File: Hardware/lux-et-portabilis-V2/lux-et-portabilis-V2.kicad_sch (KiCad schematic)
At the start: 45 parts, among them J1 Conn_01x03_Socket, J2 Conn_01x03_Socket, J3 Conn_01x04_Socket, Q1 2N7002K, Q2 2N7002K, Q3 PMOS, U1 ESP32-C3-Supermini, U2 TP4056

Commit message: Fabrication files for Lux et Portabilis V2
Added power saving by shutting down the battery
Added onboard boot button
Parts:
- C1, C3: LCSC C2162971 -> C25170691
- C4, C6: LCSC C77075 -> C15850
- C5: LCSC C380331 -> C15850
- D1: LCSC C2909920 -> C2480
- J3: footprint Custom_Footprints:MPU6050 -> Aleoexpress:MPU6050
- PORT1, PORT2: LCSC 1 -> C7433470
- R1, R12, R2: value 2k2 -> 2.2k
- R14, R15: LCSC C60491 -> C149504
- U1: footprint Custom_Footprints:ESP32-C3-Supermini -> Aleoexpress:ESP32-C3-Supermini
- U2: footprint Custom_Footprints:ESOP-8_L4.9-W3.9-P1.27-LS6.0-BL-EP -> Aleoexpress:ESOP-8_L4.9-W3.9-P1.27-LS6.0-BL-EP; Manufacturer Part TP4056 -> (none)

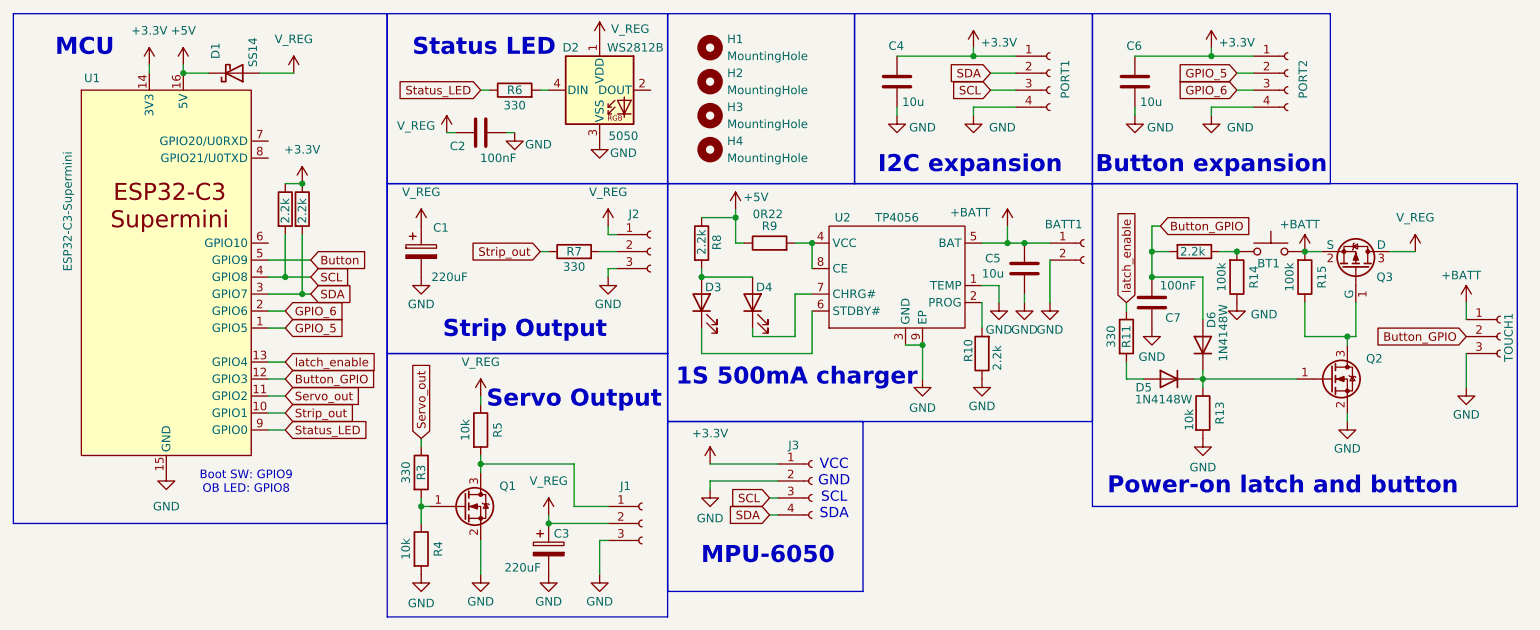
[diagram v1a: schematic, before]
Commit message: Added ADC reading to Portabilis V2
Plus board render
Changed Status LED pin to GPIO10
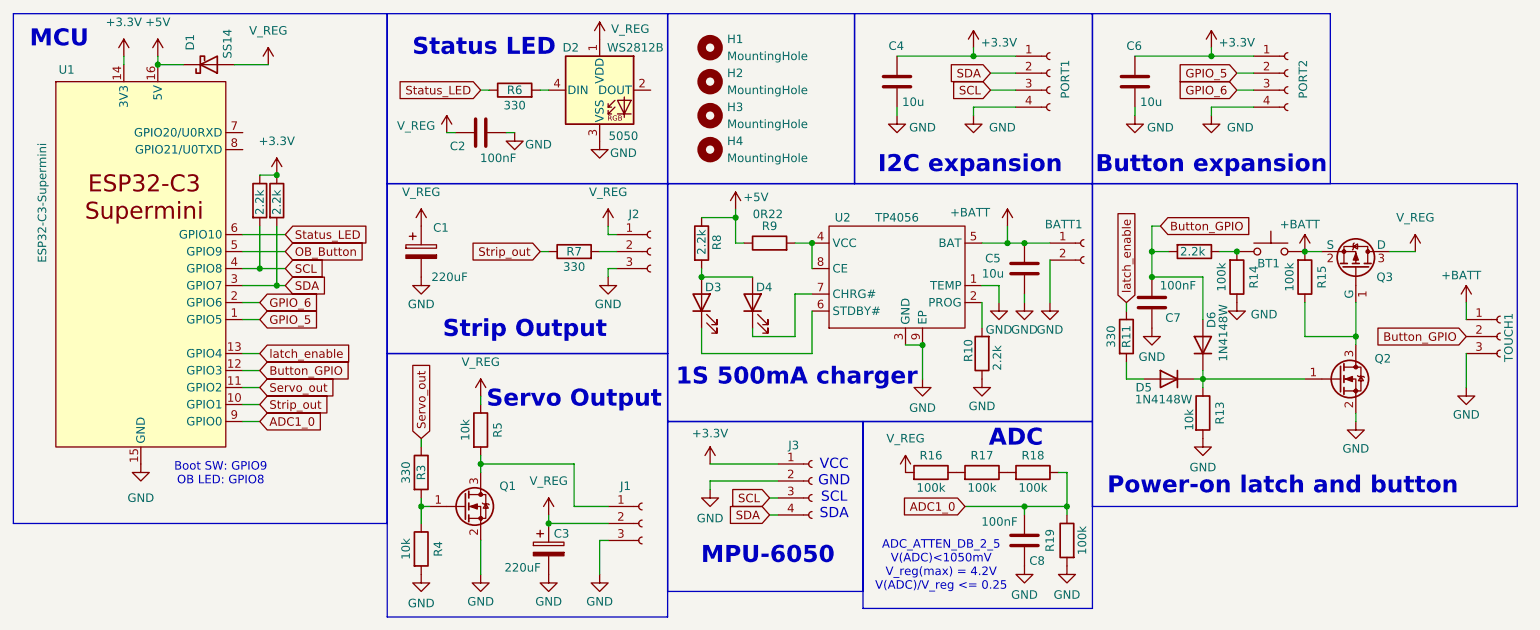
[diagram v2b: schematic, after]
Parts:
- added C8: 100nF, Capacitor_SMD:C_0805_2012Metric, symbol Device:C
- added R16, R17, R18, R19: 100k, Resistor_SMD:R_0805_2012Metric, symbol Device:R
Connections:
- net GND: now also C8.1, R19.2
- net Status_LED: now also U1.6 (GPIO10); no longer U1.9 (GPIO0)
- net V_REG: now also R16.2
- net Button renamed OB_Button
- new net: R17.1, R18.2
- new net: R16.1, R17.2
- new net ADC1_0: C8.2, R18.1, R19.1, U1.9 (GPIO0)
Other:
- note added: "ADC"
- note added: "ADC_ATTEN_DB_2_5 V(ADC)<1050mV V_reg(max) = 4.2V V(ADC)/V_reg <= 0.25"
- moved on the sheet: D1, Q2, U1

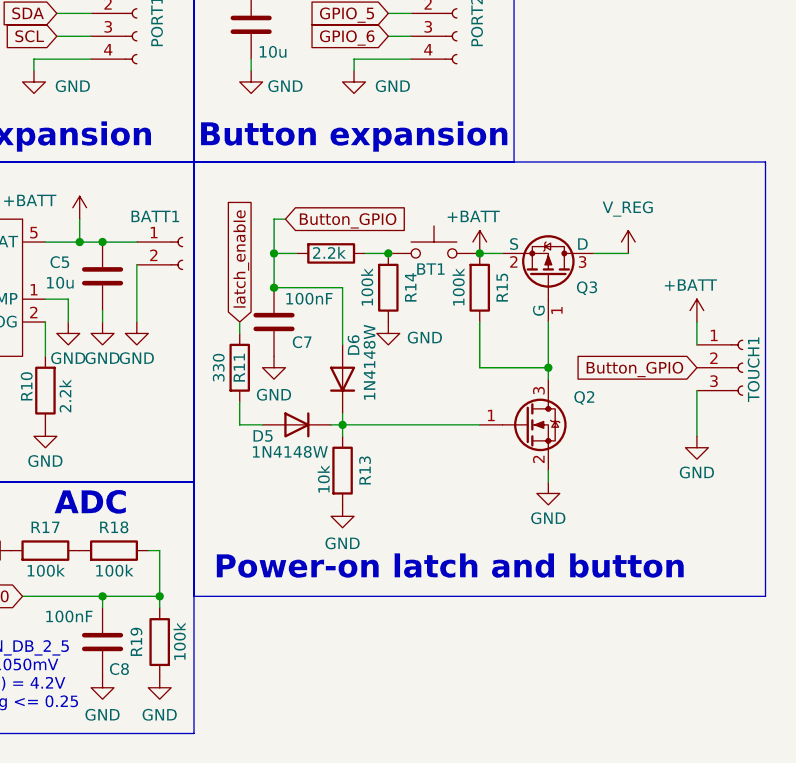
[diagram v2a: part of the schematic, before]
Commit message: Added power latch explanation
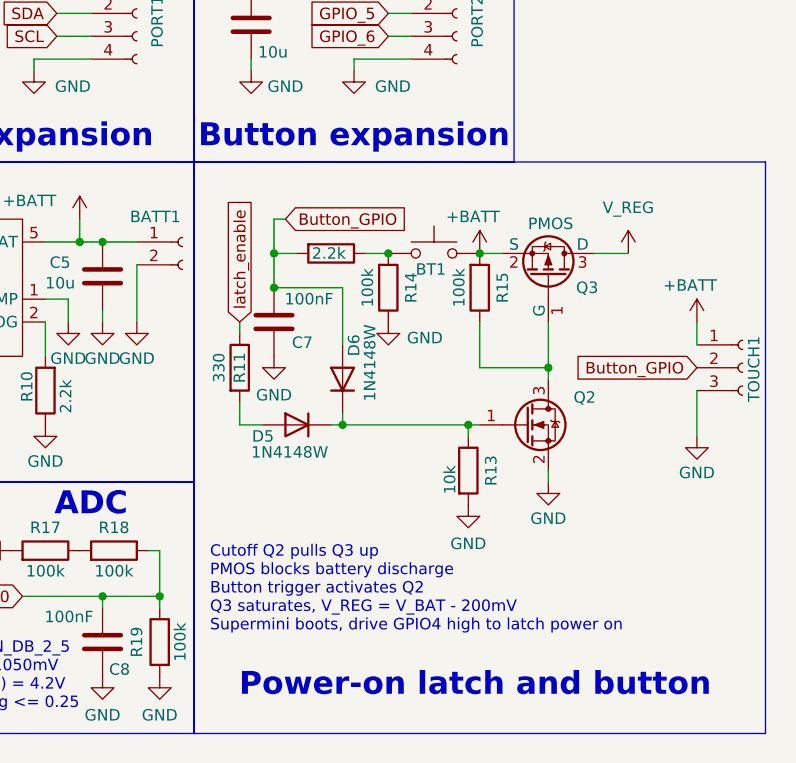
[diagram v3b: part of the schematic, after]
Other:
- note added: "Cutoff Q2 pulls Q3 up PMOS blocks battery discharge Button trigger activates Q2 Q3 saturates, V_REG = V_BAT - 200mV Supermini boots, drive GPIO4 high to latch power on"
- moved on the sheet: R13
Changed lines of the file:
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@@
 	(rectangle
 		(start 176.53 40.64)
-		(end 240.03 88.9)
+		(end 240.03 104.14)
 		(stroke
 			(width 0)
@@
 	(text "Power-on latch and button"
 		(exclude_from_sim no)
-		(at 204.978 85.852 0)
+		(at 207.772 98.806 0)
 		(effects
 			(font
@@
 		)
 	)
+	(text "Cutoff Q2 pulls Q3 up\nPMOS blocks battery discharge\nButton trigger activates Q2\nQ3 saturates, V_REG = V_BAT - 200mV\nSupermini boots, drive GPIO4 high to latch power on"
+		(exclude_from_sim no)
+		(at 178.308 88.138 0)
+		(effects
+			(font
+				(size 1.27 1.27)
+			)
+			(justify left)
+		)
+	)
 	(text "1S 500mA charger"
 		(exclude_from_sim no)
@@
 	)
 	(junction
+		(at 207.01 69.85)
+		(diameter 0)
+		(color 0 0 0 0)
+	)
+	(junction
 		(at 54.61 55.88)
 		(diameter 0)
@@
 	(wire
 		(pts
+			(xy 207.01 69.85) (xy 193.04 69.85)
+		)
+		(stroke
+			(width 0)
+			(type default)
+		)
+	)
+	(wire
+		(pts
 			(xy 194.31 21.59) (xy 200.66 21.59)
 		)
@@
 	(wire
 		(pts
-			(xy 193.04 69.85) (xy 208.28 69.85)
-		)
-		(stroke
-			(width 0)
-			(type default)
-		)
-	)
-	(wire
-		(pts
 			(xy 208.28 50.8) (xy 210.82 50.8)
 		)
@@
 	(wire
 		(pts
-			(xy 193.04 71.12) (xy 193.04 69.85)
+			(xy 207.01 71.12) (xy 207.01 69.85)
 		)
 		(stroke
@@
 	(wire
 		(pts
+			(xy 207.01 69.85) (xy 208.28 69.85)
+		)
+		(stroke
+			(width 0)
+			(type default)
+		)
+	)
+	(wire
+		(pts
 			(xy 151.13 64.77) (xy 151.13 69.85)
 		)
@@
 	(symbol
 		(lib_id "power:GND")
-		(at 193.04 78.74 0)
+		(at 207.01 78.74 0)
 		(unit 1)
 		(exclude_from_sim no)
@@
 		(dnp no)
 		(property "Reference" "#PWR034"
-			(at 193.04 85.09 0)
+			(at 207.01 85.09 0)
 			(effects
 				(font
@@
 		)
 		(property "Value" "GND"
-			(at 193.04 83.058 0)
+			(at 207.01 83.058 0)
 			(effects
 				(font
@@
 		)
 		(property "Footprint" ""
-			(at 193.04 78.74 0)
+			(at 207.01 78.74 0)
 			(effects
 				(font
@@
 		)
 		(property "Datasheet" ""
-			(at 193.04 78.74 0)
+			(at 207.01 78.74 0)
 			(effects
 				(font
@@
 		)
 		(property "Description" "Power symbol creates a global label with name \"GND\" , ground"
-			(at 193.04 78.74 0)
+			(at 207.01 78.74 0)
 			(effects
 				(font
@@
 	(symbol
 		(lib_id "Device:R")
-		(at 193.04 74.93 0)
+		(at 207.01 74.93 0)
 		(unit 1)
 		(exclude_from_sim no)
@@
 		(dnp no)
 		(property "Reference" "R13"
-			(at 195.58 74.93 90)
+			(at 209.55 74.93 90)
 			(effects
 				(font
@@
 		)
 		(property "Value" "10k"
-			(at 191.008 75.946 90)
+			(at 204.978 75.946 90)
 			(effects
 				(font
@@
 		)
 		(property "Footprint" "Resistor_SMD:R_0805_2012Metric"
-			(at 191.262 74.93 90)
+			(at 205.232 74.93 90)
 			(effects
 				(font
@@
 		)
 		(property "Datasheet" "~"
-			(at 193.04 74.93 0)
+			(at 207.01 74.93 0)
 			(effects
 				(font
@@
 		)
 		(property "Description" "Resistor"
-			(at 193.04 74.93 0)
+			(at 207.01 74.93 0)
 			(effects
 				(font
@@
 		)
 		(property "LCSC" "C17414"
-			(at 193.04 74.93 90)
+			(at 207.01 74.93 90)
 			(effects
 				(font
@@
 		)
 		(property "ASSEMBLY" ""
-			(at 193.04 74.93 0)
+			(at 207.01 74.93 0)
 			(effects
 				(font
@@
 		)
 		(property "SUPPLIER 1" ""
-			(at 193.04 74.93 0)
+			(at 207.01 74.93 0)
 			(effects
 				(font
@@
 		)
 		(property "SUPPLIER 2" ""
-			(at 193.04 74.93 0)
+			(at 207.01 74.93 0)
 			(effects
 				(font
@@
 		)
 		(property "Value" "PMOS"
-			(at 217.17 43.688 90)
+			(at 216.154 47.498 90)
 			(effects
 				(font
 					(size 1.27 1.27)
 				)
-				(hide yes)
 			)
 		)

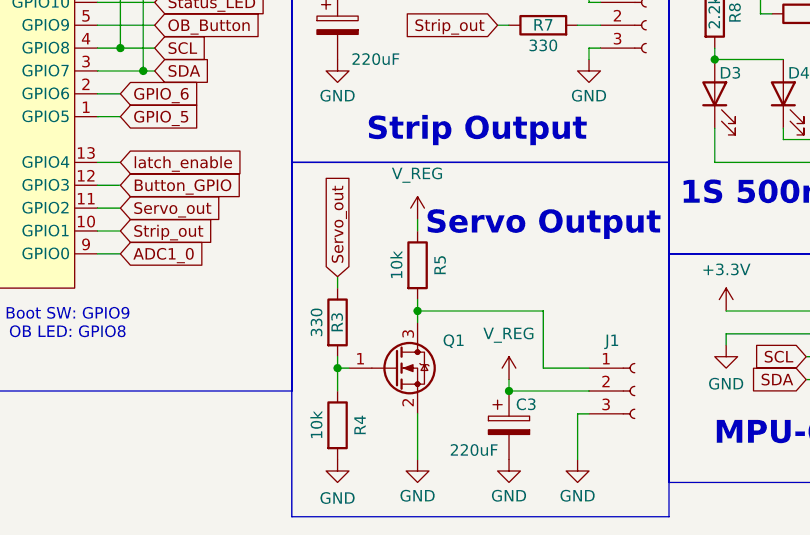
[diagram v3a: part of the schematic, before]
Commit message: Added Marajoara V2 - ESP32 + I2S Audio
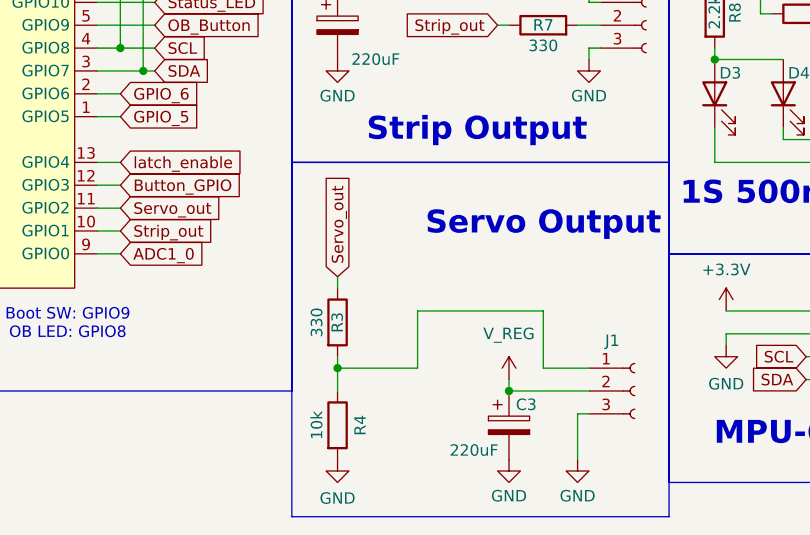
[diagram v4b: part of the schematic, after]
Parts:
- removed Q1: 2N7002K, Package_TO_SOT_SMD:SOT-23, symbol Transistor_FET:2N7002K
- removed R5: 10k, Resistor_SMD:R_0805_2012Metric, symbol Device:R
- R9: footprint Resistor_SMD:R_2010_5025Metric -> Resistor_SMD:R_1206_3216Metric_Pad1.30x1.75mm_HandSolder; LCSC C2999625 -> C2683384
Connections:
- net at R3.2, R4.1: now also J1.1 (Pin_1)
